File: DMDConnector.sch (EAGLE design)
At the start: 7 parts

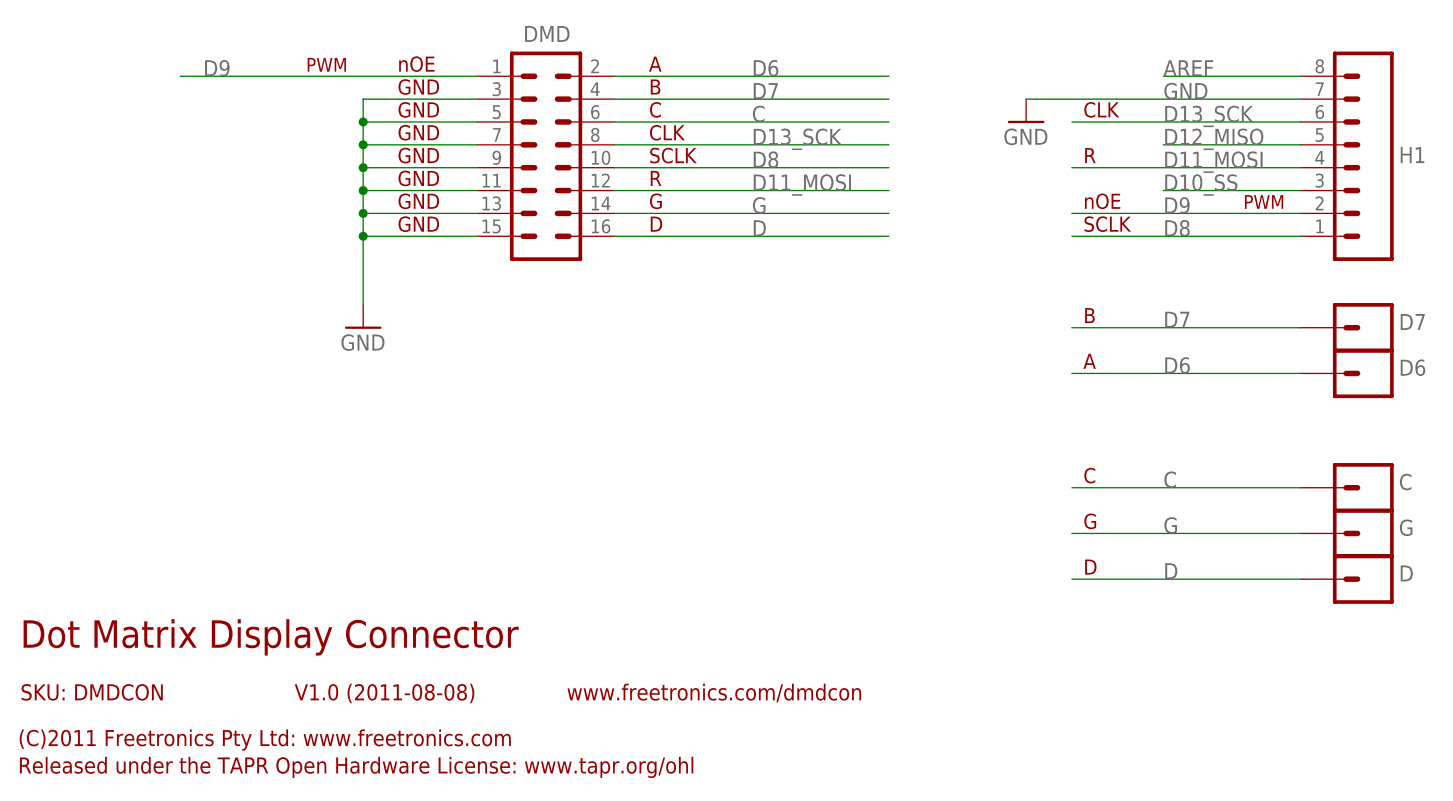
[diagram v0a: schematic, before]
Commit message: Rename nOE line to OE, add pulldown resistor, bump version to V1.1
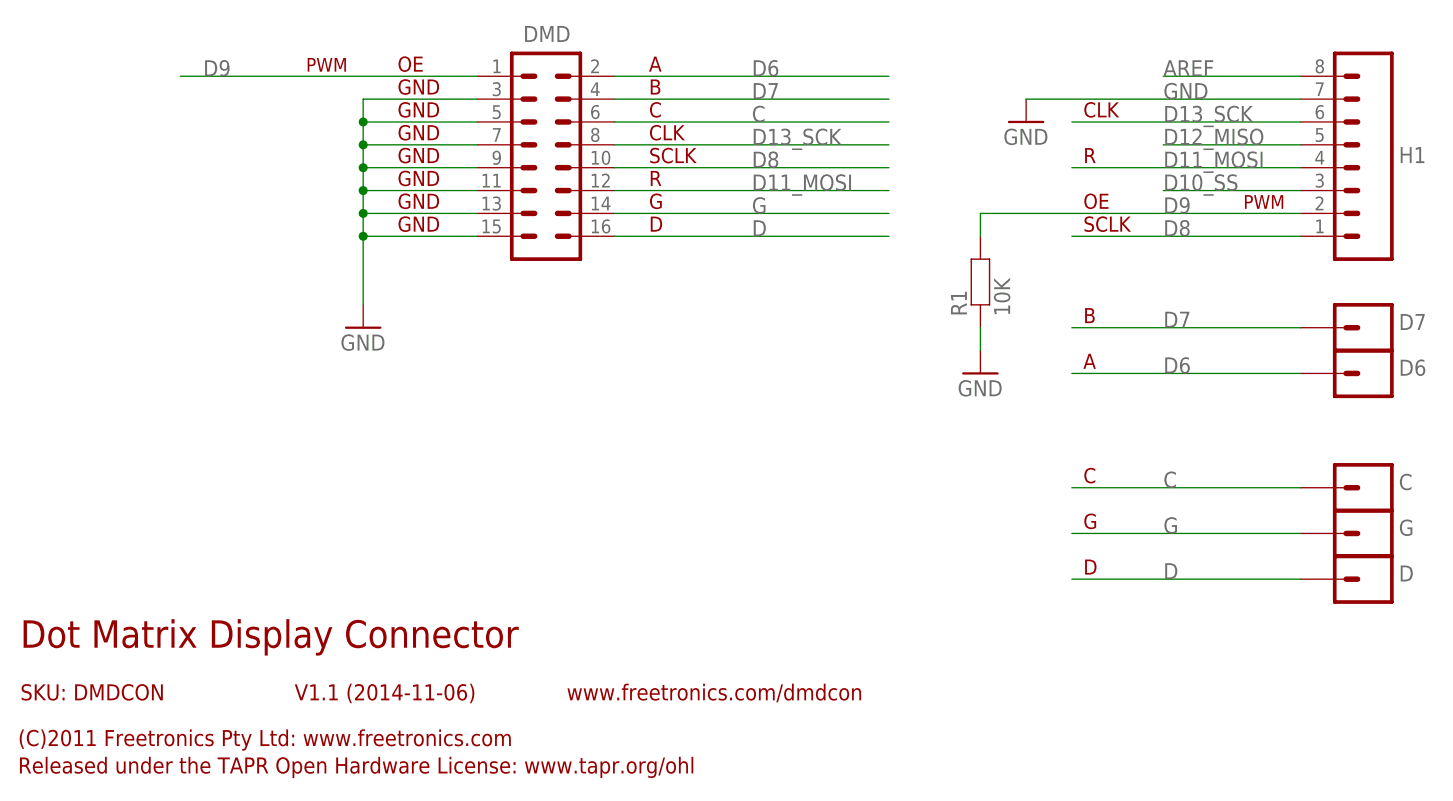
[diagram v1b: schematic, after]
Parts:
- added R1: 10K, freetronics-master-v1.1:RESISTOR0805
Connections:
- net D9: now also R1.2
- net GND: now also R1.1
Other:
- note added: "OE"
- note added: "V1.1 (2014-11-06)"
- note removed: "V1.0 (2011-08-08)"
- note removed: "nOE"
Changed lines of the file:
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@@
 <part name="G" library="freetronics-master-v1" deviceset="M01" device="PTH"/>
 <part name="D" library="freetronics-master-v1" deviceset="M01" device="PTH"/>
+<part name="R1" library="freetronics-master-v1.1" deviceset="RESISTOR" device="0805" value="10K"/>
+<part name="GND3" library="freetronics" deviceset="GND" device=""/>
 </parts>
 <sheets>
@@
 <plain>
 <text x="7.62" y="20.32" size="3.048" layer="94">Dot Matrix Display Connector</text>
-<text x="38.1" y="14.478" size="1.778" layer="94">V1.0 (2011-08-08)</text>
+<text x="38.1" y="14.478" size="1.778" layer="94">V1.1 (2014-11-06)</text>
 <text x="7.62" y="14.478" size="1.778" layer="94">SKU: DMDCON</text>
 <text x="7.366" y="9.398" size="1.778" layer="94">(C)2011 Freetronics Pty Ltd: www.freetronics.com</text>
 <text x="7.366" y="6.35" size="1.778" layer="94">Released under the TAPR Open Hardware License: www.tapr.org/ohl</text>
 <text x="68.326" y="14.478" size="1.778" layer="94">www.freetronics.com/dmdcon</text>
-<text x="49.53" y="84.328" size="1.6764" layer="94" ratio="10">nOE</text>
+<text x="49.53" y="84.328" size="1.6764" layer="94" ratio="10">OE</text>
 <text x="49.53" y="81.788" size="1.6764" layer="94" ratio="10">GND</text>
 <text x="49.53" y="79.248" size="1.6764" layer="94" ratio="10">GND</text>
@@
 <text x="77.47" y="71.628" size="1.6764" layer="94" ratio="10">R</text>
 <text x="143.51" y="69.088" size="1.524" layer="94" ratio="10">PWM</text>
-<text x="125.73" y="69.088" size="1.6764" layer="94" ratio="10">nOE</text>
+<text x="125.73" y="69.088" size="1.6764" layer="94" ratio="10">OE</text>
 <text x="125.73" y="51.308" size="1.6764" layer="94" ratio="10">A</text>
 <text x="125.73" y="56.388" size="1.6764" layer="94" ratio="10">B</text>
@@
 <attribute name="NAME" x="160.782" y="27.686" size="1.778" layer="95"/>
 </instance>
+<instance part="R1" gate="G$1" x="114.3" y="60.96" rot="R90"/>
+<instance part="GND3" gate="1" x="114.3" y="50.8"/>
 </instances>
 <busses>
@@
 <pinref part="GND2" gate="1" pin="GND"/>
 </segment>
+<segment>
+<pinref part="R1" gate="G$1" pin="1"/>
+<wire x1="114.3" y1="55.88" x2="114.3" y2="53.34" width="0.1524" layer="91"/>
+<pinref part="GND3" gate="1" pin="GND"/>
+</segment>
 </net>
 <net name="AREF" class="0">
@@
 <net name="D9" class="0">
 <segment>
-<wire x1="124.46" y1="68.58" x2="149.86" y2="68.58" width="0.1524" layer="91"/>
+<wire x1="114.3" y1="68.58" x2="149.86" y2="68.58" width="0.1524" layer="91"/>
 <label x="134.62" y="68.58" size="1.778" layer="95"/>
 <pinref part="H1" gate="G$1" pin="2"/>
+<pinref part="R1" gate="G$1" pin="2"/>
+<wire x1="114.3" y1="68.58" x2="114.3" y2="66.04" width="0.1524" layer="91"/>
 </segment>
 <segment>
@@
 </sheet>
 </sheets>
+<errors>
+</errors>
 </schematic>
 </drawing>
